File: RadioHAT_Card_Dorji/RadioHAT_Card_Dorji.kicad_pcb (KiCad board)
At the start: 2 copper layers, 30 x 51 mm, 10 parts, among them J2 Conn_Coaxial, J3 Conn_Coaxial, J4 Conn_Coaxial, J5 Conn_Coaxial, J6 Conn_Coaxial

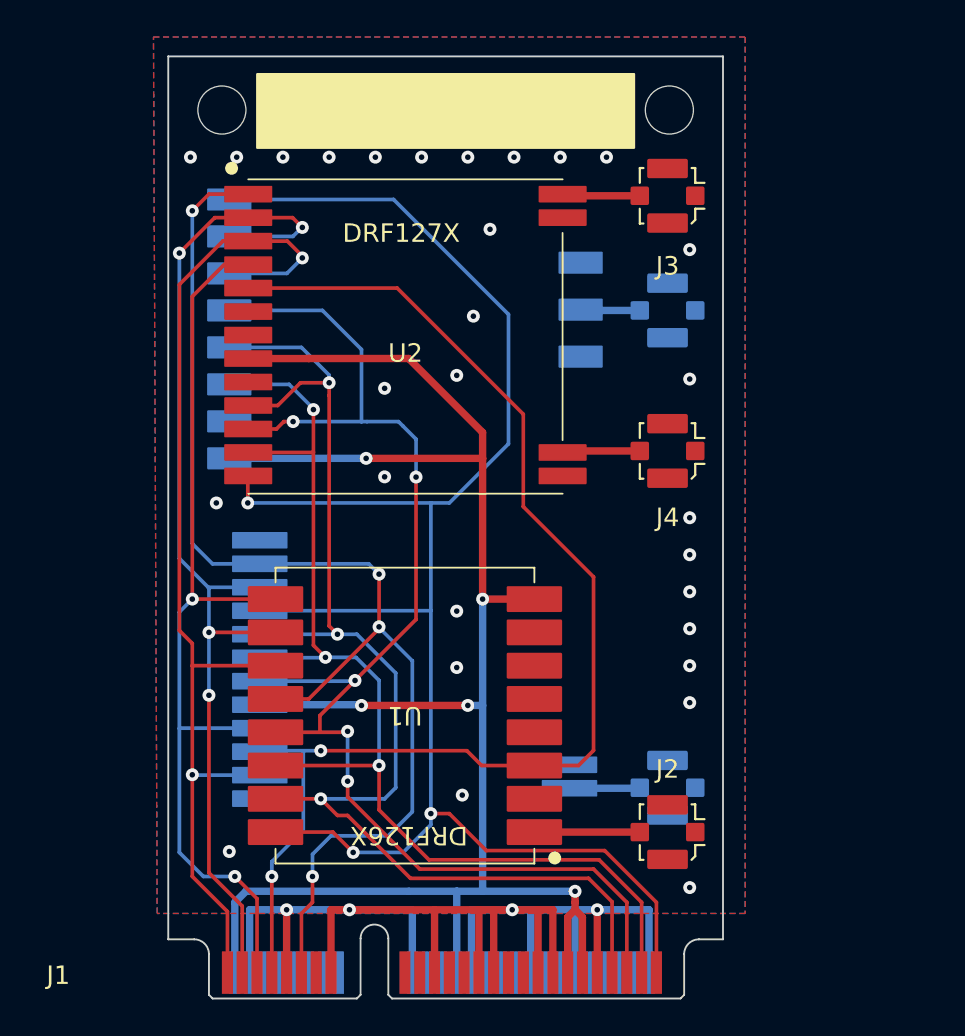
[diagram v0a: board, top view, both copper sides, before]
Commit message: [PCB] Adjust radio position to move coax connector away from screw
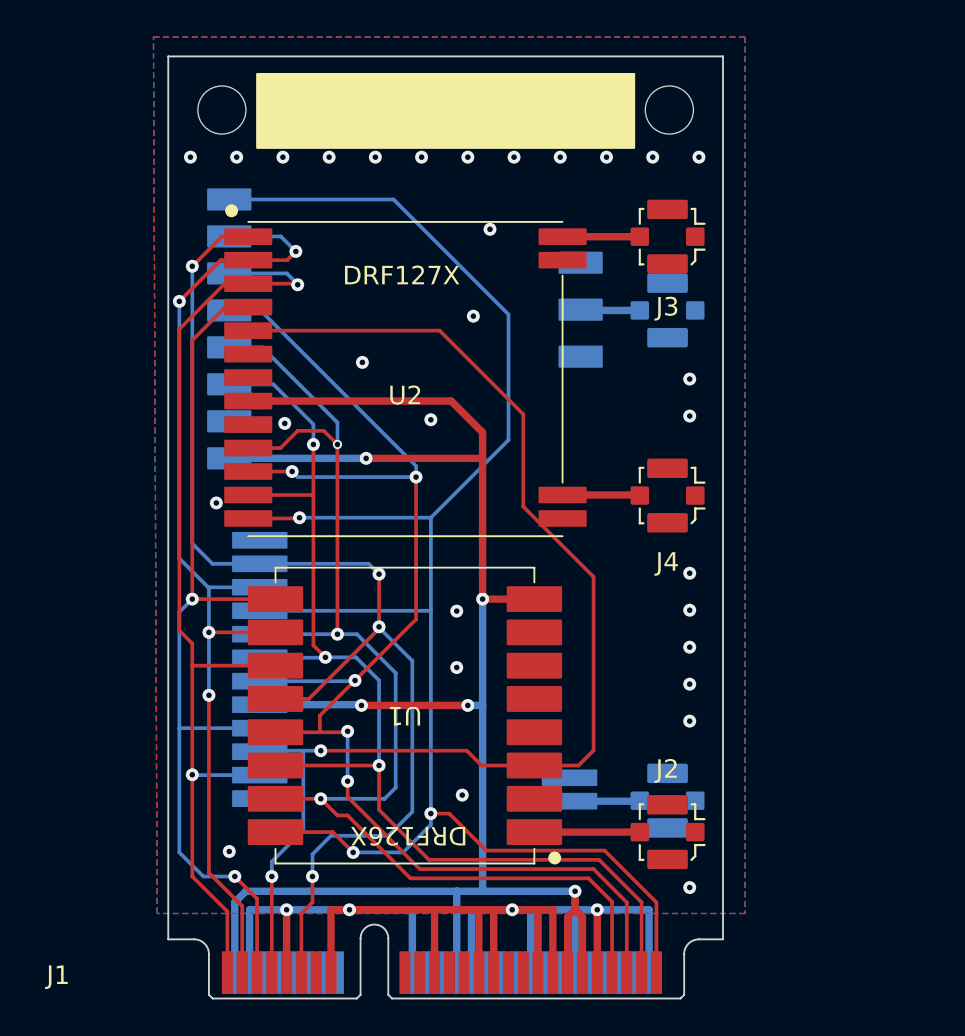
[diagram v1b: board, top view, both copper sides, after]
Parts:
- moved J4 2.41 mm to (144.8, 92.8)
- moved U2 2.30 mm to (130.6, 86.5)
- moved J3 2.21 mm to (144.8, 78.8)
- moved J6 0.70 mm to (144.8, 109.3)
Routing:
- net IRQ0: track 58.9 -> 55.5 mm
- net RST0: track 66.1 -> 63.3 mm
- net IRQ1: track 52.2 -> 49.9 mm
- net NSS: track 96.2 -> 94.0 mm
- net GPIO0: track 60.8 -> 58.7 mm
- net +3V3: track 102.8 -> 101.8 mm
- net GPIO1: track 68.9 -> 67.9 mm
- net SCK: track 68.6 -> 68.0 mm
- net GND: vias 33 -> 34

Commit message: [PCB] Minor Dorji card fixes from rev0
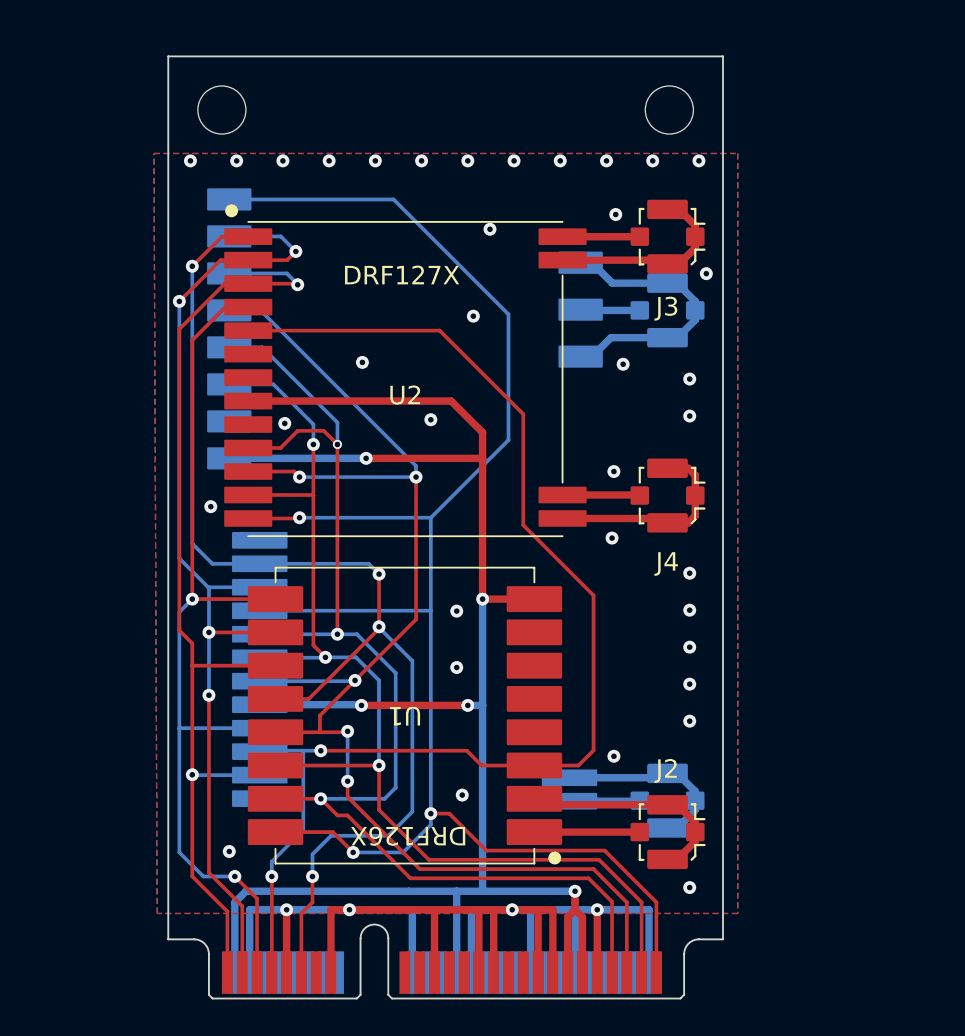
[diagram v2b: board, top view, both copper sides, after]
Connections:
- J2 pad 2: GND -> Net-(J2-Ext)
- J3 pad 2: GND -> Net-(J3-Ext)
- J4 pad 2: GND -> Net-(J4-Ext)
- J5 pad 2: GND -> Net-(J5-Ext)
- J6 pad 2: GND -> Net-(J6-Ext)
- U1 pad 2: GND -> Net-(J2-Ext)
- U2 pad 14: GND -> Net-(J4-Ext)
- U2 pad 16: GND -> Net-(J3-Ext)
- U3 pad 11: GND -> Net-(J5-Ext)
- U3 pad 9: GND -> Net-(J5-Ext)
- U4 pad 14: GND -> Net-(J6-Ext)
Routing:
- net Net-(J5-Ext): track 0.00 -> 15.1 mm
- net Net-(J2-Ext): track 0.00 -> 12.1 mm
- net Net-(J4-Ext): track 0.00 -> 11.3 mm
- net Net-(J3-Ext): track 0.00 -> 10.7 mm
- net Net-(J6-Ext): track 0.00 -> 10.2 mm
- net GND: vias 34 -> 40

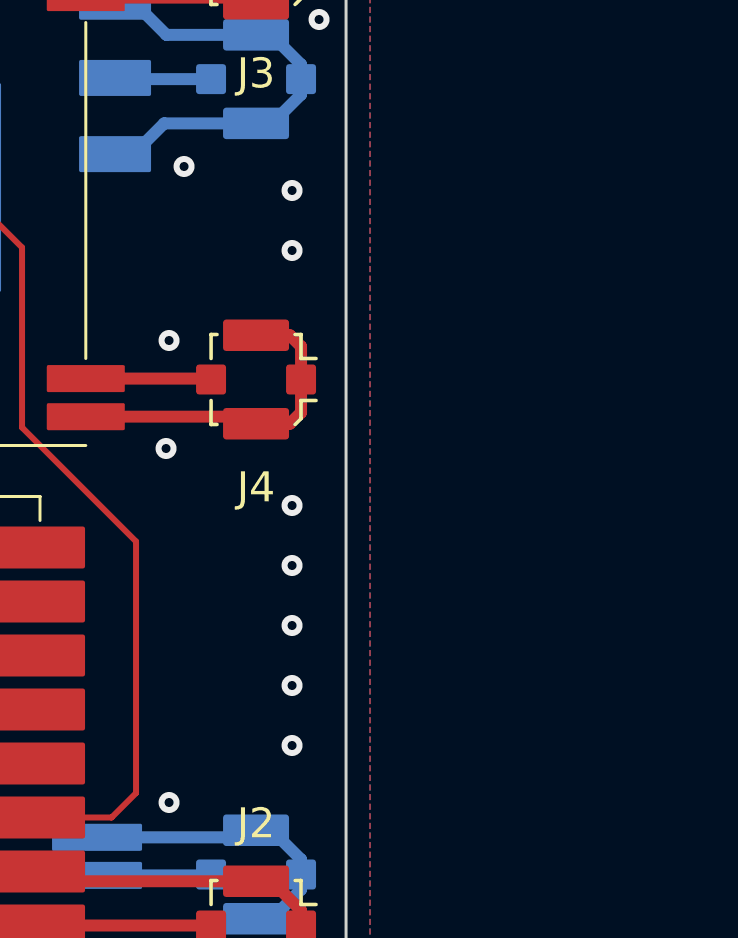
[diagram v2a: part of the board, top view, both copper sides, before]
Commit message: [PCB] Rework modules to isolate antenna ground
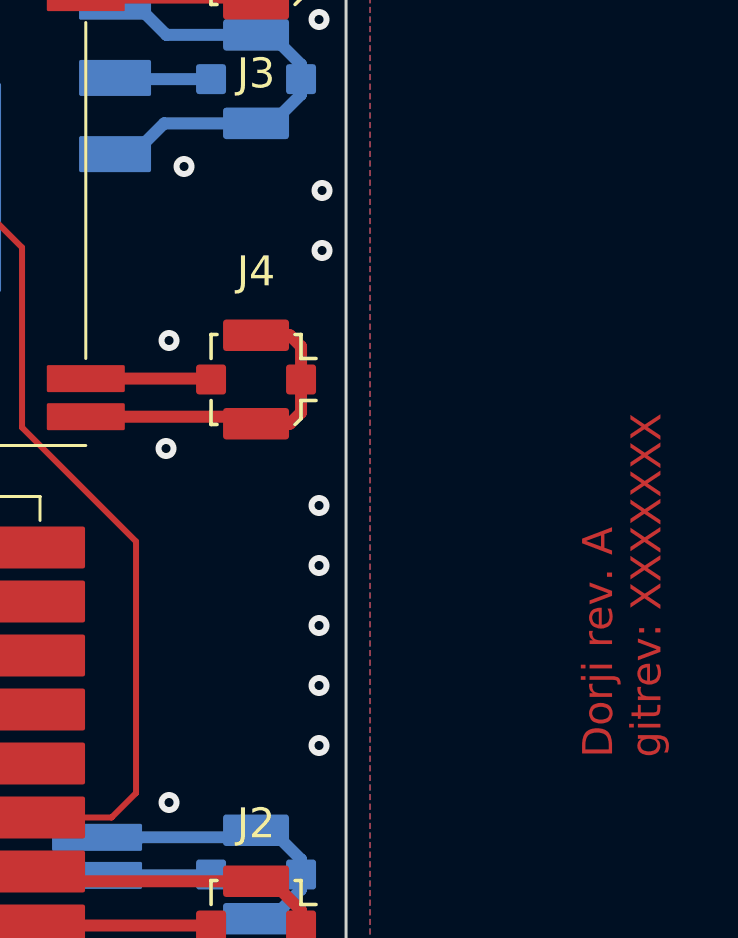
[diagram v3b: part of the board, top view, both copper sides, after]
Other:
- board text added: "Dorji rev. A gitrev: XXXXXXX"
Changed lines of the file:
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@@
 		(tags "mcrf hirose ufl u.fl microcoaxial")
 		(property "Reference" "J4"
-			(at 3.6 0 0)
+			(at -3.6 0 0)
 			(layer "F.SilkS")
 			(effects
@@
 		)
 		(fp_text user "${REFERENCE}"
-			(at -3.4 0 0)
+			(at 3.3 0 0)
 			(layer "F.Fab")
 			(effects
@@
 		)
 	)
+	(gr_text "Dorji rev. A\ngitrev: XXXXXXX"
+		(at 158.4 105.4 90)
+		(layer "F.Cu")
+		(effects
+			(font
+				(size 1 1)
+				(thickness 0.15)
+			)
+			(justify left bottom)
+		)
+	)
 	(dimension
 		(type orthogonal)
@@
 	)
 	(via
-		(at 146 105)
+		(at 146.9 105)
 		(size 0.7)
 		(drill 0.3)
@@
 	)
 	(via
-		(at 146 103)
+		(at 146.9 103)
 		(size 0.7)
 		(drill 0.3)
@@
 	)
 	(via
-		(at 146 101)
+		(at 146.9 101)
 		(size 0.7)
 		(drill 0.3)
@@
 	)
 	(via
-		(at 146 88.5)
+		(at 147 88.5)
 		(size 0.7)
 		(drill 0.3)
@@
 	)
 	(via
-		(at 146 97)
+		(at 146.9 97)
 		(size 0.7)
 		(drill 0.3)
@@
 	)
 	(via
-		(at 146 99)
+		(at 146.9 99)
 		(size 0.7)
 		(drill 0.3)
@@
 	)
 	(via
-		(at 146 86.5)
+		(at 147 86.5)
 		(size 0.7)
 		(drill 0.3)

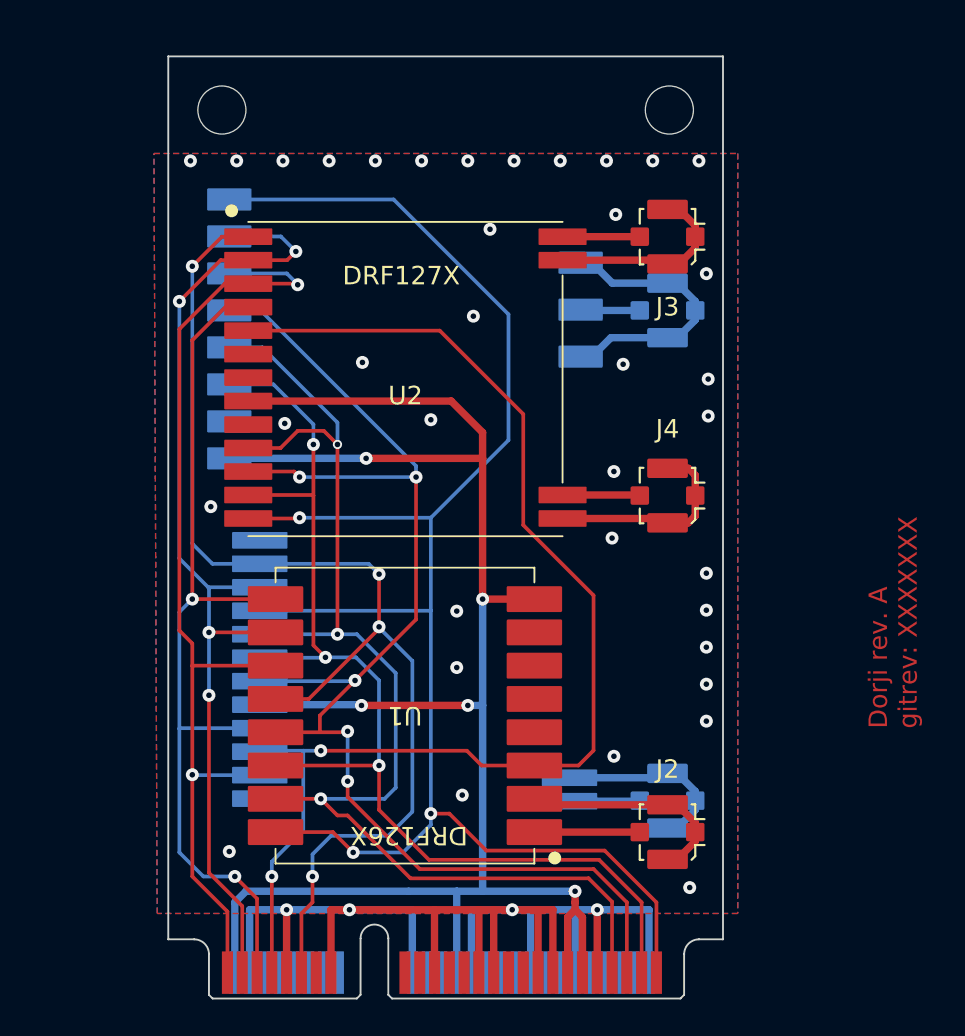
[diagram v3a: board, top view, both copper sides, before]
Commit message: [PCB] Cleanup, move text
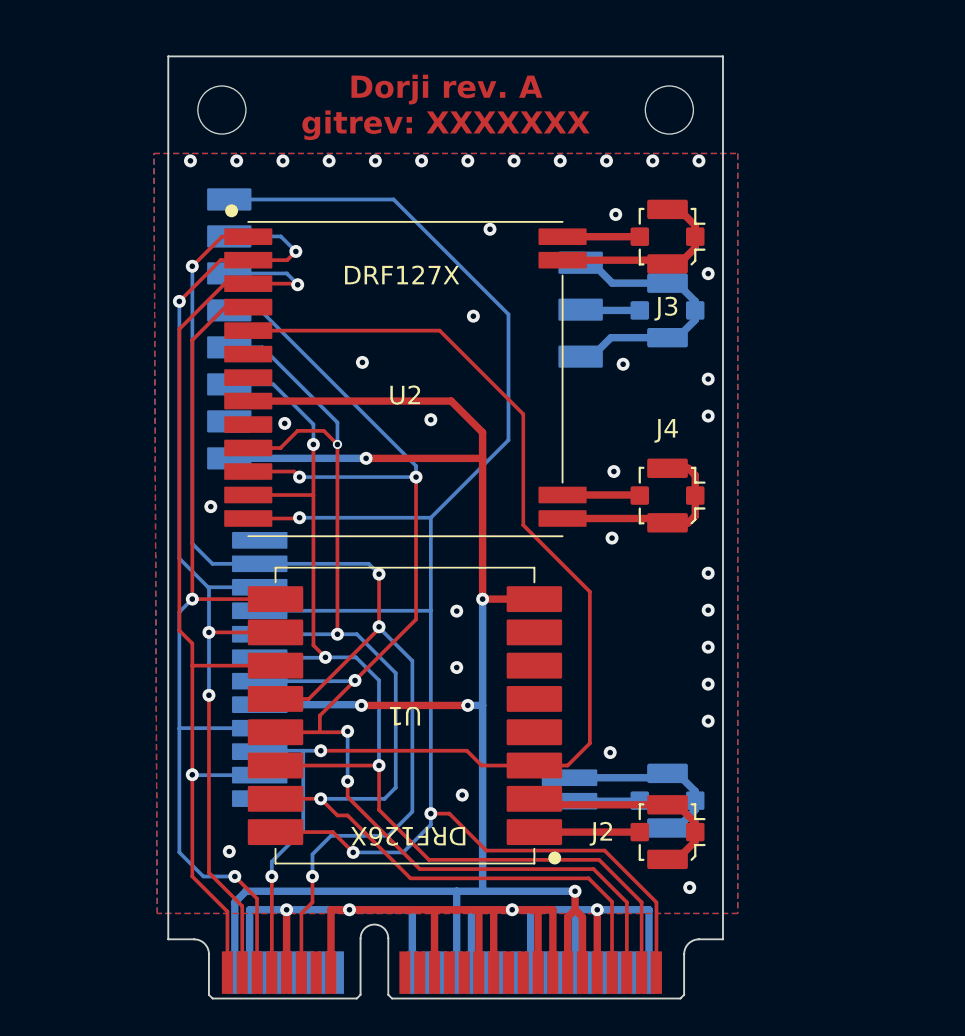
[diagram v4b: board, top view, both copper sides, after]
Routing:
- net GPIO0: track 58.7 -> 56.3 mm
- net GPIO1: track 67.9 -> 67.4 mm
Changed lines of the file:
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@@
 		(allow_soldermask_bridges_in_footprints no)
 		(tenting front back)
+		(grid_origin 117.8 120)
 		(pcbplotparams
 			(layerselection 0x00000000_00000000_55555555_5755f5ff)
@@
 		(tags "mcrf hirose ufl u.fl microcoaxial")
 		(property "Reference" "J2"
-			(at -3.4 0 0)
+			(at 0 3.5 0)
 			(layer "F.SilkS")
 			(effects
@@
 	)
 	(gr_text "Dorji rev. A\ngitrev: XXXXXXX"
-		(at 158.4 105.4 90)
+		(at 132.8 71.7 0)
 		(layer "F.Cu")
 		(effects
 			(font
-				(size 1 1)
-				(thickness 0.15)
+				(size 1.2 1.2)
+				(thickness 0.25)
+				(bold yes)
 			)
-			(justify left bottom)
 		)
 	)
@@
 	)
 	(via
-		(at 146.9 105)
+		(at 147 105)
 		(size 0.7)
 		(drill 0.3)
@@
 	)
 	(via
-		(at 146.9 103)
+		(at 147 103)
 		(size 0.7)
 		(drill 0.3)
@@
 	)
 	(via
-		(at 146.9 101)
+		(at 147 101)
 		(size 0.7)
 		(drill 0.3)
@@
 	)
 	(via
-		(at 146.9 80.8)
+		(at 147 80.8)
 		(size 0.7)
 		(drill 0.3)
@@
 	)
 	(via
-		(at 146.9 97)
+		(at 147 97)
 		(size 0.7)
 		(drill 0.3)
@@
 	)
 	(via
-		(at 141.9 106.9)
+		(at 141.7 106.7)
 		(size 0.7)
 		(drill 0.3)
@@
 	)
 	(via
-		(at 146.9 99)
+		(at 147 99)
 		(size 0.7)
 		(drill 0.3)
@@
 	)
 	(segment
-		(start 123.8 108.2375)
-		(end 121.425 108.2375)
-		(width 0.2)
-		(layer "B.Cu")
-		(net 2)
-	)
-	(segment
 		(start 119.12 107.92)
 		(end 122.75 107.92)
@@
 	)
 	(segment
-		(start 139.8 114.8)
-		(end 139.8 115.2)
-		(width 0.4)
-		(layer "F.Cu")
-		(net 8)
-	)
-	(segment
 		(start 140.2 115.6)
 		(end 140.2 118.6)
@@
 	)
 	(segment
-		(start 139.8 114.8)
+		(start 139.8 115.2)
 		(end 139.8 114.2)
 		(width 0.4)
@@
 	)
 	(segment
-		(start 130.8 114.2)
-		(end 133.4 114.2)
-		(width 0.4)
-		(layer "B.Cu")
-		(net 8)
-	)
-	(segment
 		(start 134.8 98.4)
 		(end 134.8 104.15)
@@
 	(segment
 		(start 122 114.2)
-		(end 130.8 114.2)
-		(width 0.4)
-		(layer "B.Cu")
-		(net 8)
-	)
-	(segment
-		(start 134.05 104.2)
-		(end 134 104.15)
+		(end 133.4 114.2)
 		(width 0.4)
 		(layer "B.Cu")
@@
 	)
 	(segment
-		(start 126.05 106.6)
-		(end 133.95 106.6)
-		(width 0.2)
-		(layer "F.Cu")
-		(net 22)
-	)
-	(segment
-		(start 123.4 113.588903)
-		(end 123.4 113.4)
+		(start 140.6 106.2)
+		(end 140.6 98)
 		(width 0.2)
 		(layer "F.Cu")
@@
 	)
 	(segment
-		(start 139.984612 107.4)
-		(end 140.8 106.584612)
+		(start 132.48 83.88)
+		(end 122.125 83.88)
 		(width 0.2)
 		(layer "F.Cu")
@@
 	)
 	(segment
-		(start 123.4 113.588903)
-		(end 123.4 118.6)
+		(start 137.6 107.4)
+		(end 139.4 107.4)
 		(width 0.2)
 		(layer "F.Cu")
@@
 	)
 	(segment
-		(start 133.95 106.6)
-		(end 134.75 107.4)
+		(start 140.6 98)
+		(end 137 94.4)
 		(width 0.2)
 		(layer "F.Cu")
@@
 	)
 	(segment
-		(start 137 88.4)
-		(end 132.48 83.88)
+		(start 126.05 106.6)
+		(end 133.95 106.6)
 		(width 0.2)
 		(layer "F.Cu")
@@
 	)
 	(segment
-		(start 132.48 83.88)
-		(end 122.125 83.88)
+		(start 123.4 118.6)
+		(end 123.4 113.4)
 		(width 0.2)
 		(layer "F.Cu")
@@
 	)
 	(segment
-		(start 137 94.4)
-		(end 137 88.4)
+		(start 133.95 106.6)
+		(end 134.75 107.4)
 		(width 0.2)
 		(layer "F.Cu")
@@
 	)
 	(segment
-		(start 134.75 107.4)
-		(end 137.6 107.4)
+		(start 137 88.4)
+		(end 132.48 83.88)
 		(width 0.2)
 		(layer "F.Cu")
@@
 	)
 	(segment
-		(start 137.6 107.4)
-		(end 139.984612 107.4)
+		(start 137 94.4)
+		(end 137 88.4)
 		(width 0.2)
 		(layer "F.Cu")
@@
 	)
 	(segment
-		(start 140.8 106.584612)
-		(end 140.8 98.2)
+		(start 134.75 107.4)
+		(end 137.6 107.4)
 		(width 0.2)
 		(layer "F.Cu")
@@
 	)
 	(segment
-		(start 140.8 98.2)
-		(end 137 94.4)
+		(start 139.4 107.4)
+		(end 140.6 106.2)
 		(width 0.2)
 		(layer "F.Cu")
@@
 	)
 	(segment
-		(start 139.54 82.7875)
-		(end 139.5 82.7475)
-		(width 0.4)
-		(layer "B.Cu")
-		(net 27)
-	)
-	(segment

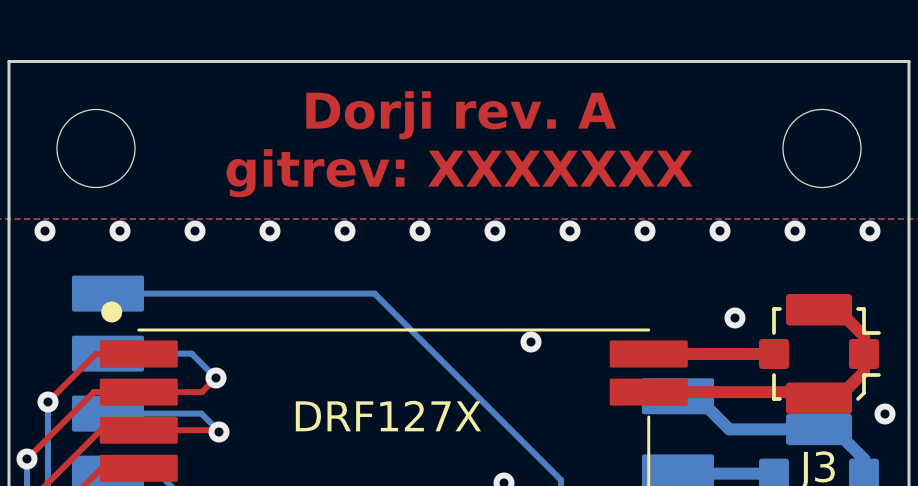
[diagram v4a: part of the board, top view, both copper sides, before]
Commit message: [PCB] Finalize labels
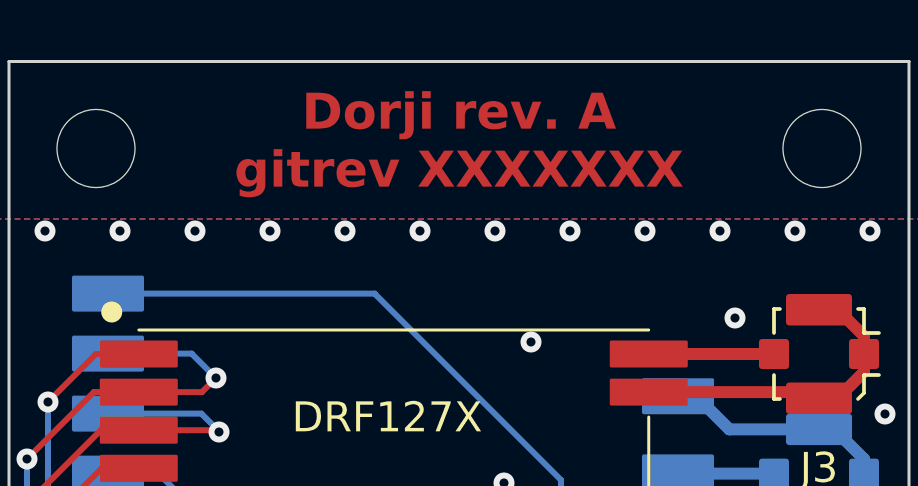
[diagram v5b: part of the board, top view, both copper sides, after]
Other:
- board text added: "Dorji rev. A gitrev XXXXXXX"
- board text removed: "Dorji rev. A gitrev: XXXXXXX"
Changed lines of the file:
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@@
 		)
 	)
-	(gr_text "Dorji rev. A\ngitrev: XXXXXXX"
+	(gr_text "Dorji rev. A\ngitrev XXXXXXX"
 		(at 132.8 71.7 0)
 		(layer "F.Cu")
